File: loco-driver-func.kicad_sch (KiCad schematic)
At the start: 5 parts, among them Q901 BSS138, Q902 BSS138

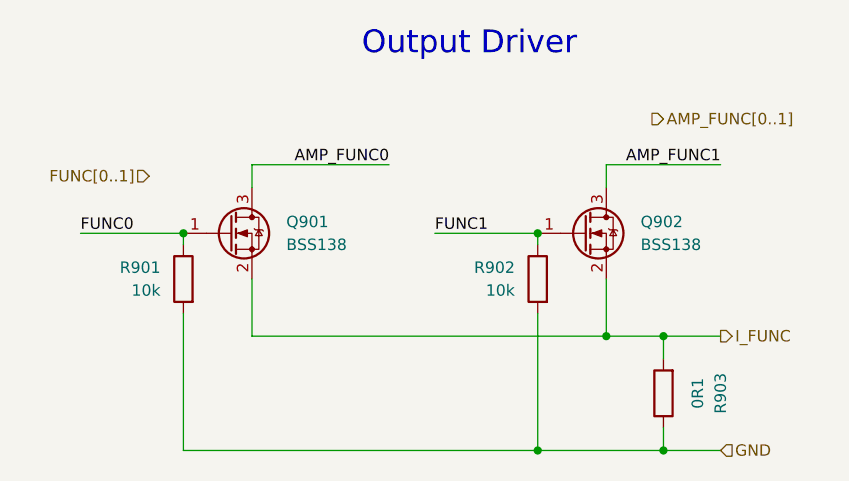
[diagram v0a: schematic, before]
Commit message: Fix - Remove ERC error, refresh annotation
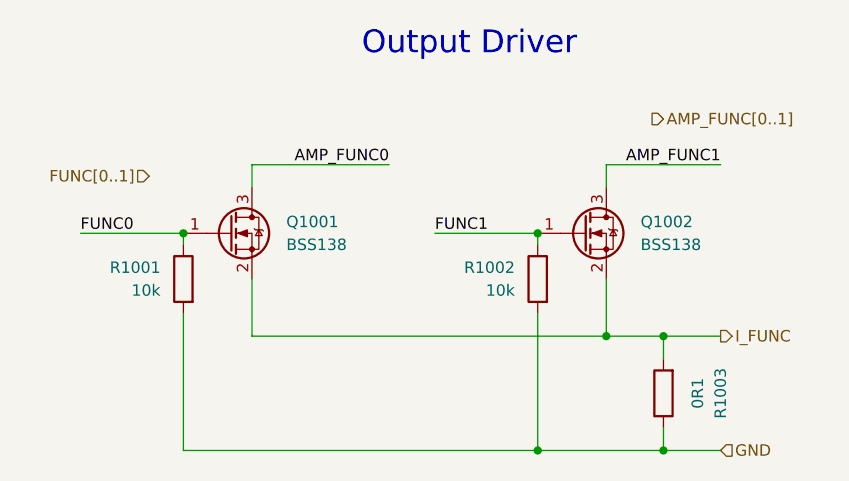
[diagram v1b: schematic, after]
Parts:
- renumbered Q901 to Q1001, Q902 to Q1002, R901 to R1001, R902 to R1002, R903 to R1003
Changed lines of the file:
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@@
 		(on_board yes)
 		(dnp no)
-		(property "Reference" "R902"
+		(property "Reference" "R1002"
 			(at 76.2 59.6899 0)
 			(effects
@@
 			(project "xDuinoRails-Thor-M"
 				(path "/fb33ec4e-6596-45d2-a121-8d3475acd69a/e1a52612-70a7-429e-ada6-6f2a698a279c"
-					(reference "R902")
+					(reference "R1002")
 					(unit 1)
 				)
@@
 		(on_board yes)
 		(dnp no)
-		(property "Reference" "R903"
+		(property "Reference" "R1003"
 			(at 99.06 73.66 90)
 			(effects
@@
 			(project "xDuinoRails-Thor-M"
 				(path "/fb33ec4e-6596-45d2-a121-8d3475acd69a/e1a52612-70a7-429e-ada6-6f2a698a279c"
-					(reference "R903")
+					(reference "R1003")
 					(unit 1)
 				)
@@
 		(on_board yes)
 		(dnp no)
-		(property "Reference" "R901"
+		(property "Reference" "R1001"
 			(at 36.83 59.6899 0)
 			(effects
@@
 			(project "xDuinoRails-Thor-M"
 				(path "/fb33ec4e-6596-45d2-a121-8d3475acd69a/e1a52612-70a7-429e-ada6-6f2a698a279c"
-					(reference "R901")
+					(reference "R1001")
 					(unit 1)
 				)
@@
 		(dnp no)
 		(fields_autoplaced yes)
-		(property "Reference" "Q901"
+		(property "Reference" "Q1001"
 			(at 50.8 54.6099 0)
 			(effects
@@
 			(project "xDuinoRails-Thor-M"
 				(path "/fb33ec4e-6596-45d2-a121-8d3475acd69a/e1a52612-70a7-429e-ada6-6f2a698a279c"
-					(reference "Q901")
+					(reference "Q1001")
 					(unit 1)
 				)
@@
 		(dnp no)
 		(fields_autoplaced yes)
-		(property "Reference" "Q902"
+		(property "Reference" "Q1002"
 			(at 90.17 54.6099 0)
 			(effects
@@
 			(project "xDuinoRails-Thor-M"
 				(path "/fb33ec4e-6596-45d2-a121-8d3475acd69a/e1a52612-70a7-429e-ada6-6f2a698a279c"
-					(reference "Q902")
+					(reference "Q1002")
 					(unit 1)
 				)

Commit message: Fix - revert to working model
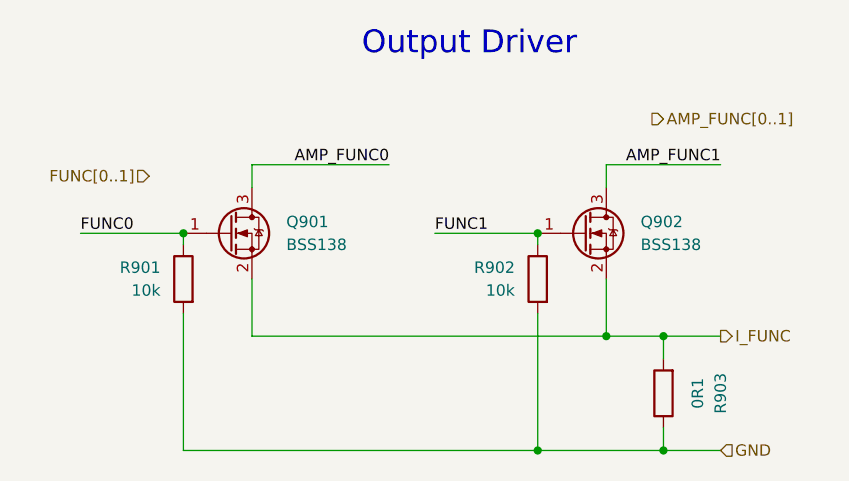
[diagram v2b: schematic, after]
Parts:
- renumbered Q1001 to Q901, Q1002 to Q902, R1001 to R901, R1002 to R902, R1003 to R903
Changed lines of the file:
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@@
 		(on_board yes)
 		(dnp no)
-		(property "Reference" "R1002"
+		(property "Reference" "R902"
 			(at 76.2 59.6899 0)
 			(effects
@@
 			(project "xDuinoRails-Thor-M"
 				(path "/fb33ec4e-6596-45d2-a121-8d3475acd69a/e1a52612-70a7-429e-ada6-6f2a698a279c"
-					(reference "R1002")
+					(reference "R902")
 					(unit 1)
 				)
@@
 		(on_board yes)
 		(dnp no)
-		(property "Reference" "R1003"
+		(property "Reference" "R903"
 			(at 99.06 73.66 90)
 			(effects
@@
 			(project "xDuinoRails-Thor-M"
 				(path "/fb33ec4e-6596-45d2-a121-8d3475acd69a/e1a52612-70a7-429e-ada6-6f2a698a279c"
-					(reference "R1003")
+					(reference "R903")
 					(unit 1)
 				)
@@
 		(on_board yes)
 		(dnp no)
-		(property "Reference" "R1001"
+		(property "Reference" "R901"
 			(at 36.83 59.6899 0)
 			(effects
@@
 			(project "xDuinoRails-Thor-M"
 				(path "/fb33ec4e-6596-45d2-a121-8d3475acd69a/e1a52612-70a7-429e-ada6-6f2a698a279c"
-					(reference "R1001")
+					(reference "R901")
 					(unit 1)
 				)
@@
 		(dnp no)
 		(fields_autoplaced yes)
-		(property "Reference" "Q1001"
+		(property "Reference" "Q901"
 			(at 50.8 54.6099 0)
 			(effects
@@
 			(project "xDuinoRails-Thor-M"
 				(path "/fb33ec4e-6596-45d2-a121-8d3475acd69a/e1a52612-70a7-429e-ada6-6f2a698a279c"
-					(reference "Q1001")
+					(reference "Q901")
 					(unit 1)
 				)
@@
 		(dnp no)
 		(fields_autoplaced yes)
-		(property "Reference" "Q1002"
+		(property "Reference" "Q902"
 			(at 90.17 54.6099 0)
 			(effects
@@
 			(project "xDuinoRails-Thor-M"
 				(path "/fb33ec4e-6596-45d2-a121-8d3475acd69a/e1a52612-70a7-429e-ada6-6f2a698a279c"
-					(reference "Q1002")
+					(reference "Q902")
 					(unit 1)
 				)
